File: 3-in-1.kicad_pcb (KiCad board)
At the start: 2 copper layers, 125 x 98 mm, 40 parts

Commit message: Silkscreen Update
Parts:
- removed the REF** at (199.6, 86.7)
- removed the REF** at (103.2, 140.7)
- added H1: MountingHole, MountingHole:MountingHole_2.7mm_M2.5, F.Cu at (206.4, 53.5)
- added H2: MountingHole, MountingHole:MountingHole_2.7mm_M2.5, F.Cu at (88.5, 53.5)
- added REF**: OSHW-Logo2_9.8x8mm_Copper, Symbol:OSHW-Logo2_9.8x8mm_Copper, F.Cu at (102.6, 141.0)
- added REF**: OSHW-Logo2_9.8x8mm_Copper, Symbol:OSHW-Logo2_9.8x8mm_Copper, B.Cu at (199.5, 86.5)
- added ROM-JP1: ROM Write Enable, Connector_PinHeader_2.54mm:PinHeader_1x02_P2.54mm_Vertical, F.Cu at (142.4, 109.7)
- moved BUS1 1.27 mm to (185.4, 129.5)
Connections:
- ROM-U5 pad 27: ~MEMW -> Net-(ROM-JP1-Pad2)
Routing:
- net Net-(ROM-JP1-Pad2): track 0.00 -> 16.5 mm
- net A17: track 133.5 -> 129.6 mm
- net +5V: track 754.2 -> 751.4 mm
- net D4: track 176.0 -> 177.9 mm
- net A13: track 45.3 -> 47.1 mm
- net A18: track 102.7 -> 104.3 mm
- net A19: track 121.2 -> 122.8 mm
- net IRQ4: track 172.9 -> 171.4 mm
- net +12V: track 147.5 -> 148.8 mm
- net RESETDRV: track 162.7 -> 163.9 mm
- net -12V: track 103.4 -> 104.6 mm
- net ~IOW: track 109.1 -> 110.3 mm
- net A6: track 110.2 -> 109.1 mm
- net Net-(BUS1-Pad50): track 0.00 -> 1.09 mm
- net A16: track 110.4 -> 109.4 mm
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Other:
- board text added: "Derrived from designs by: Sergey Kiselev, James Pearce, Adrian Black, Jacob Dorne"
- board text added: "Tandy 1000 PLUS 3-in-1 Upgrade 640kb, 96k UMB, CF, RS232 v1.7 by rkrenicki - 2019-11-18"
- board text removed: "Derrived from designs by: Sergey Kiselev, James Pearce, Adrian Black"
- board text removed: "Tandy 1000 PLUS 3-in-1 Upgrade 640kb, 96k UMB, CF, RS232 v1.6 by rkrenicki - 2019-11-12"

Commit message: Layout cleanup
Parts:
- removed the REF** at (102.6, 141.0)
- removed the REF** at (199.5, 86.5)
- added REF**: OSHW-Logo2_9.8x8mm_Copper, Symbol:OSHW-Logo2_9.8x8mm_Copper, F.Cu at (102.5, 141.1)
- added REF**: OSHW-Logo2_9.8x8mm_Copper, Symbol:OSHW-Logo2_9.8x8mm_Copper, B.Cu at (199.7, 85.3)
- H1, H2: footprint MountingHole:MountingHole_2.7mm_M2.5 -> MountingHole:MountingHole_2.7mm_M2.5_ISO7380_Pad
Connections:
- H1 pad 1: Net-(H1-Pad1) -> GND
- H2 pad 1: Net-(H2-Pad1) -> GND
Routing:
- net A13: track 47.1 -> 49.0 mm
- net A3: track 146.4 -> 145.0 mm
- net RESETDRV: track 163.9 -> 162.7 mm
- net A2: track 135.7 -> 136.5 mm
- net GND: vias 201 -> 203
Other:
- board text added: "Tandy 1000 PLUS 3-in-1 Upgrade 640kb, 96k UMB, CF, RS232 v1.7 by rkrenicki - 2019-11-19"
- board text removed: "Tandy 1000 PLUS 3-in-1 Upgrade 640kb, 96k UMB, CF, RS232 v1.7 by rkrenicki - 2019-11-18"

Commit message: v1.7a update
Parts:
- moved REF** 90.8 mm to (190.9, 120.2)
- moved RAM-U12 8.90 mm to (88.7, 86.3)
- moved C12 8.90 mm to (96.3, 82.9)
- moved C13 8.90 mm to (96.5, 109.9)
- moved RAM-U13 8.90 mm to (88.8, 113.2)
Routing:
- net A19: track 122.8 -> 138.4 mm
- net MEM-CE: track 76.9 -> 86.7 mm
- net A15: track 97.0 -> 106.6 mm
- net A17: track 129.6 -> 137.0 mm
- net Net-(RAM-U12-Pad2): track 16.1 -> 22.1 mm
- net A16: track 109.4 -> 113.0 mm, vias 0 -> 1
- net +5V: track 751.4 -> 754.7 mm
- net A18: track 104.3 -> 107.0 mm
- net Net-(RAM-U12-Pad10): track 34.7 -> 37.2 mm
- net AEN: track 167.4 -> 165.7 mm
- net D6: track 180.6 -> 182.0 mm
- net GND: track 12.2 -> 12.4 mm, vias 203 -> 207
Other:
- board text added: "Layout and Design by Rob Krenicki -- Derrived from designs by -- Sergey Kiselev, James Pearce, Adrian Black, Jacob Dorne"
- board text added: "Tandy 1000 EX/HX 3-in-1 Upgrade 640kb, 96k UMB, CF, RS232 Rob Krenicki - 2019-11-21 v1.7a"
- board text removed: "Derrived from designs by: Sergey Kiselev, James Pearce, Adrian Black, Jacob Dorne"
- board text removed: "Tandy 1000 PLUS 3-in-1 Upgrade 640kb, 96k UMB, CF, RS232 v1.7 by rkrenicki - 2019-11-19"

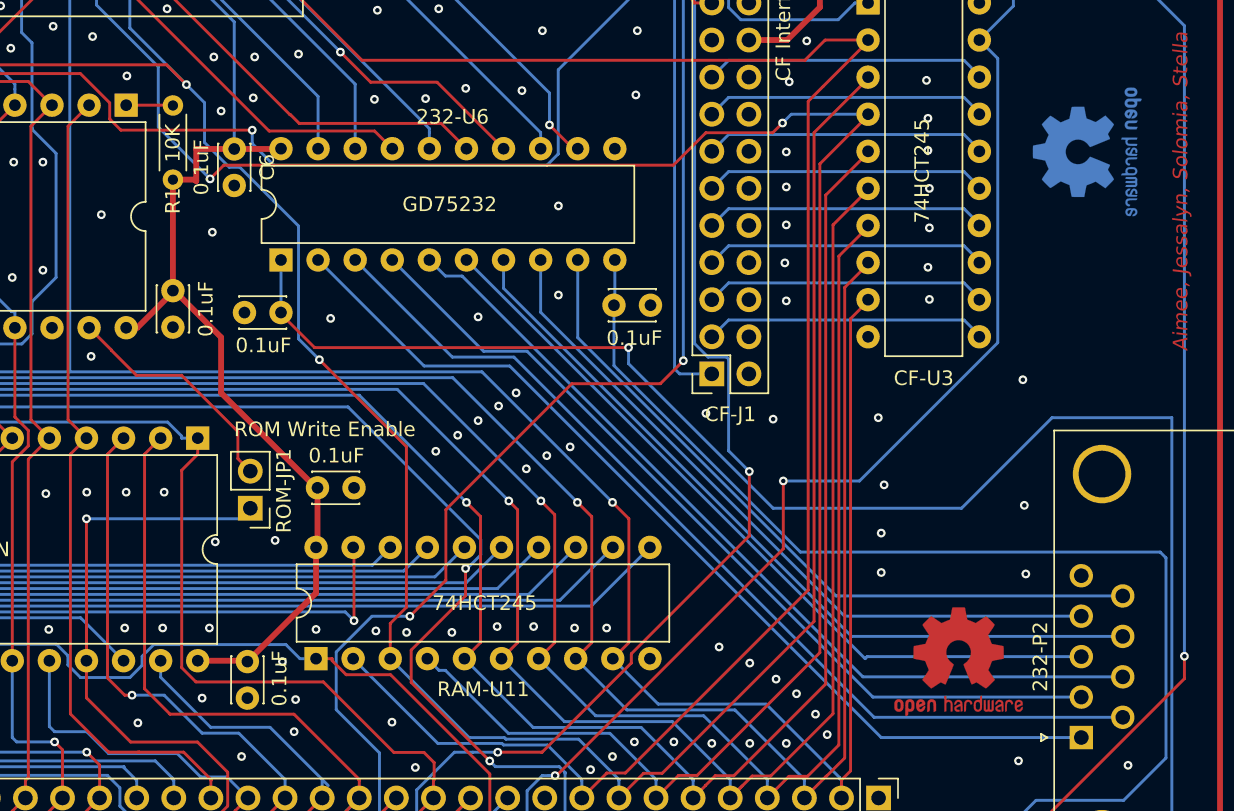
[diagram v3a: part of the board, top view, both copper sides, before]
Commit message: Pull-up Resistor added
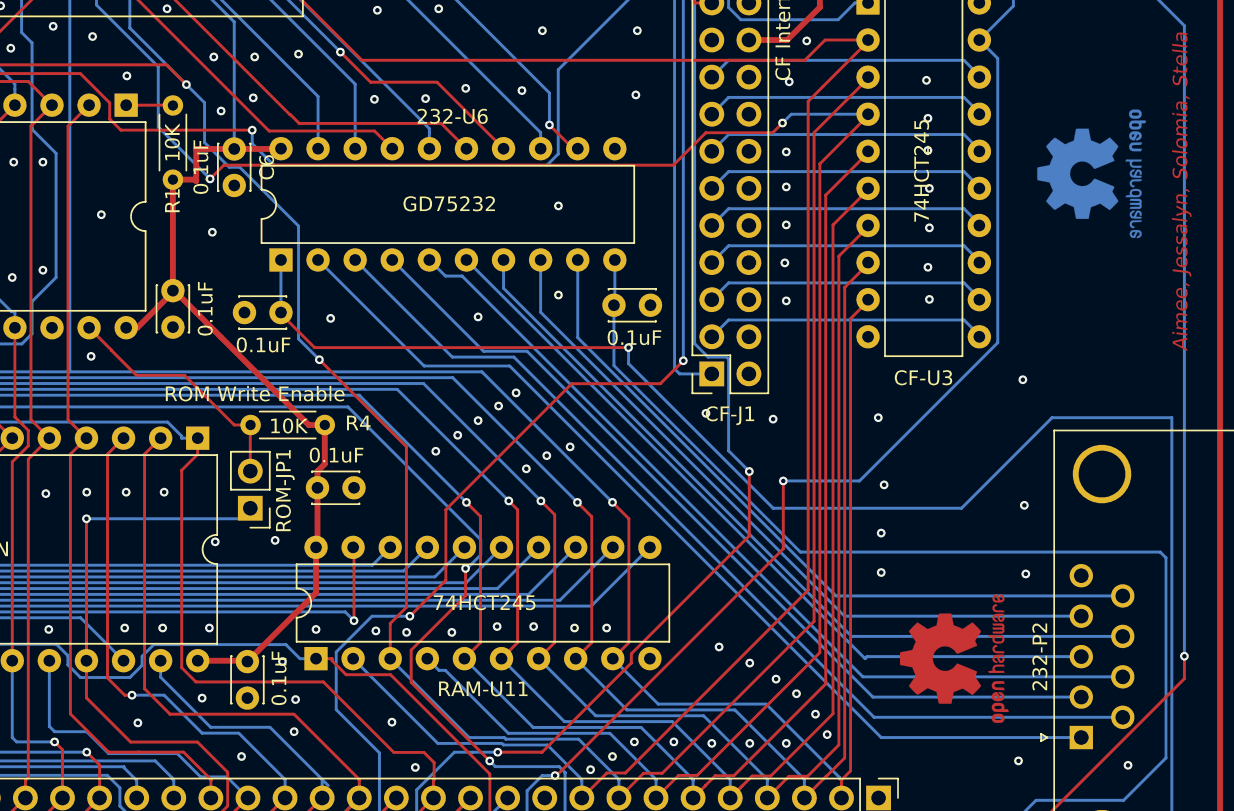
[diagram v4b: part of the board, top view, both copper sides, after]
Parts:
- removed the REF** at (190.9, 120.2)
- removed the REF** at (199.7, 85.3)
- added R4: 10K, Resistor_THT:R_Axial_DIN0204_L3.6mm_D1.6mm_P5.08mm_Horizontal, F.Cu at (147.5, 104.0)
- added REF**: OSHW-Logo2_9.8x8mm_Copper, Symbol:OSHW-Logo2_9.8x8mm_Copper, B.Cu at (200.0, 86.8)
- added REF**: OSHW-Logo2_9.8x8mm_Copper, Symbol:OSHW-Logo2_9.8x8mm_Copper, F.Cu at (190.6, 120.0)
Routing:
- net +5V: track 754.7 -> 755.7 mm
- net Net-(R4-Pad2): track 16.5 -> 17.3 mm

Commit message: 1.8 update
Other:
- board text added: "Tandy 1000 EX/HX 3-in-1 Upgrade 640kb, 96k UMB, CF, RS232 Rob Krenicki - 2019-12-01 v1.8"
- board text removed: "Tandy 1000 EX/HX 3-in-1 Upgrade 640kb, 96k UMB, CF, RS232 Rob Krenicki - 2019-11-21 v1.7a"
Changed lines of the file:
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@@
   )
   (setup
-    (last_trace_width 0.4)
+    (last_trace_width 0.2)
     (user_trace_width 0.2)
     (user_trace_width 0.4)
@@
     )
   )
-  (gr_text "Tandy 1000 EX/HX 3-in-1 Upgrade\n640kb, 96k UMB, CF, RS232\nRob Krenicki - 2019-11-21 v1.7a" (at 99.2 141.1) (layer F.Mask)
+  (gr_text "Tandy 1000 EX/HX 3-in-1 Upgrade\n640kb, 96k UMB, CF, RS232\nRob Krenicki - 2019-12-01 v1.8" (at 99.2 141.1) (layer F.Mask)
     (effects (font (size 1.3 0.83) (thickness 0.2)))
   )
@@
     (effects (font (size 1 1) (thickness 0.25) italic))
   )
-  (gr_text "Tandy 1000 EX/HX 3-in-1 Upgrade\n640kb, 96k UMB, CF, RS232\nRob Krenicki - 2019-11-21 v1.7a\n" (at 99.2 141.1) (layer F.Cu)
+  (gr_text "Tandy 1000 EX/HX 3-in-1 Upgrade\n640kb, 96k UMB, CF, RS232\nRob Krenicki - 2019-12-01 v1.8\n" (at 99.2 141.1) (layer F.Cu)
     (effects (font (size 1.3 0.83) (thickness 0.2)))
   )

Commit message: Version 1.9 Update
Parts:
- 232-U8: value 16550 -> 16C550
- CF-U3, RAM-U11: value 74HCT245 -> 74LS245
- moved R3 10.00 mm to (169.3, 80.1), turned to 90 degrees
- moved R1 7.57 mm to (142.7, 82.1), turned to 180 degrees
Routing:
- net +12V: track 148.8 -> 131.1 mm
- net Net-(CF-U1-Pad1): track 129.4 -> 147.0 mm
- net RESETDRV: track 162.7 -> 175.5 mm, vias 3 -> 2
- net D2: track 175.1 -> 185.8 mm
- net A3: track 145.0 -> 155.4 mm, vias 1 -> 0
- net D0: track 173.1 -> 182.3 mm, vias 2 -> 1
- net +5V: track 755.7 -> 764.3 mm, vias 0 -> 1
- net D3: track 193.7 -> 202.3 mm
- net A18: track 107.0 -> 112.1 mm
- net D6: track 182.0 -> 187.0 mm
- net ~IOW: track 110.3 -> 115.0 mm
- net D4: track 177.9 -> 182.6 mm
- net A0: track 91.1 -> 95.7 mm
- net D5: track 173.1 -> 177.6 mm
- net Net-(232-U6-Pad16): track 40.1 -> 44.6 mm
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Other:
- board text added: "Tandy 1000 EX/HX 3-in-1 Upgrade 640kb, 96k UMB, CF, RS232 Rob Krenicki - 2020-02-13 v1.9"
- board text removed: "Tandy 1000 EX/HX 3-in-1 Upgrade 640kb, 96k UMB, CF, RS232 Rob Krenicki - 2019-12-01 v1.8"

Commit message: Update to KiCAD 9
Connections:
- net ~IOR renamed ~{IOR}
- net ~IOW renamed ~{IOW}
- net ~MEMR renamed ~{MEMR}
- net ~MEMW renamed ~{MEMW}
- net ~ROM_CS renamed ~{ROM_CS}
- net ~UART_CS renamed ~{UART_CS}
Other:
- net class Default removed
